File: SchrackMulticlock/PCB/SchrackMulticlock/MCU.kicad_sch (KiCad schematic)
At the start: 3 parts, among them U6 ESP32-S3-WROOM-2

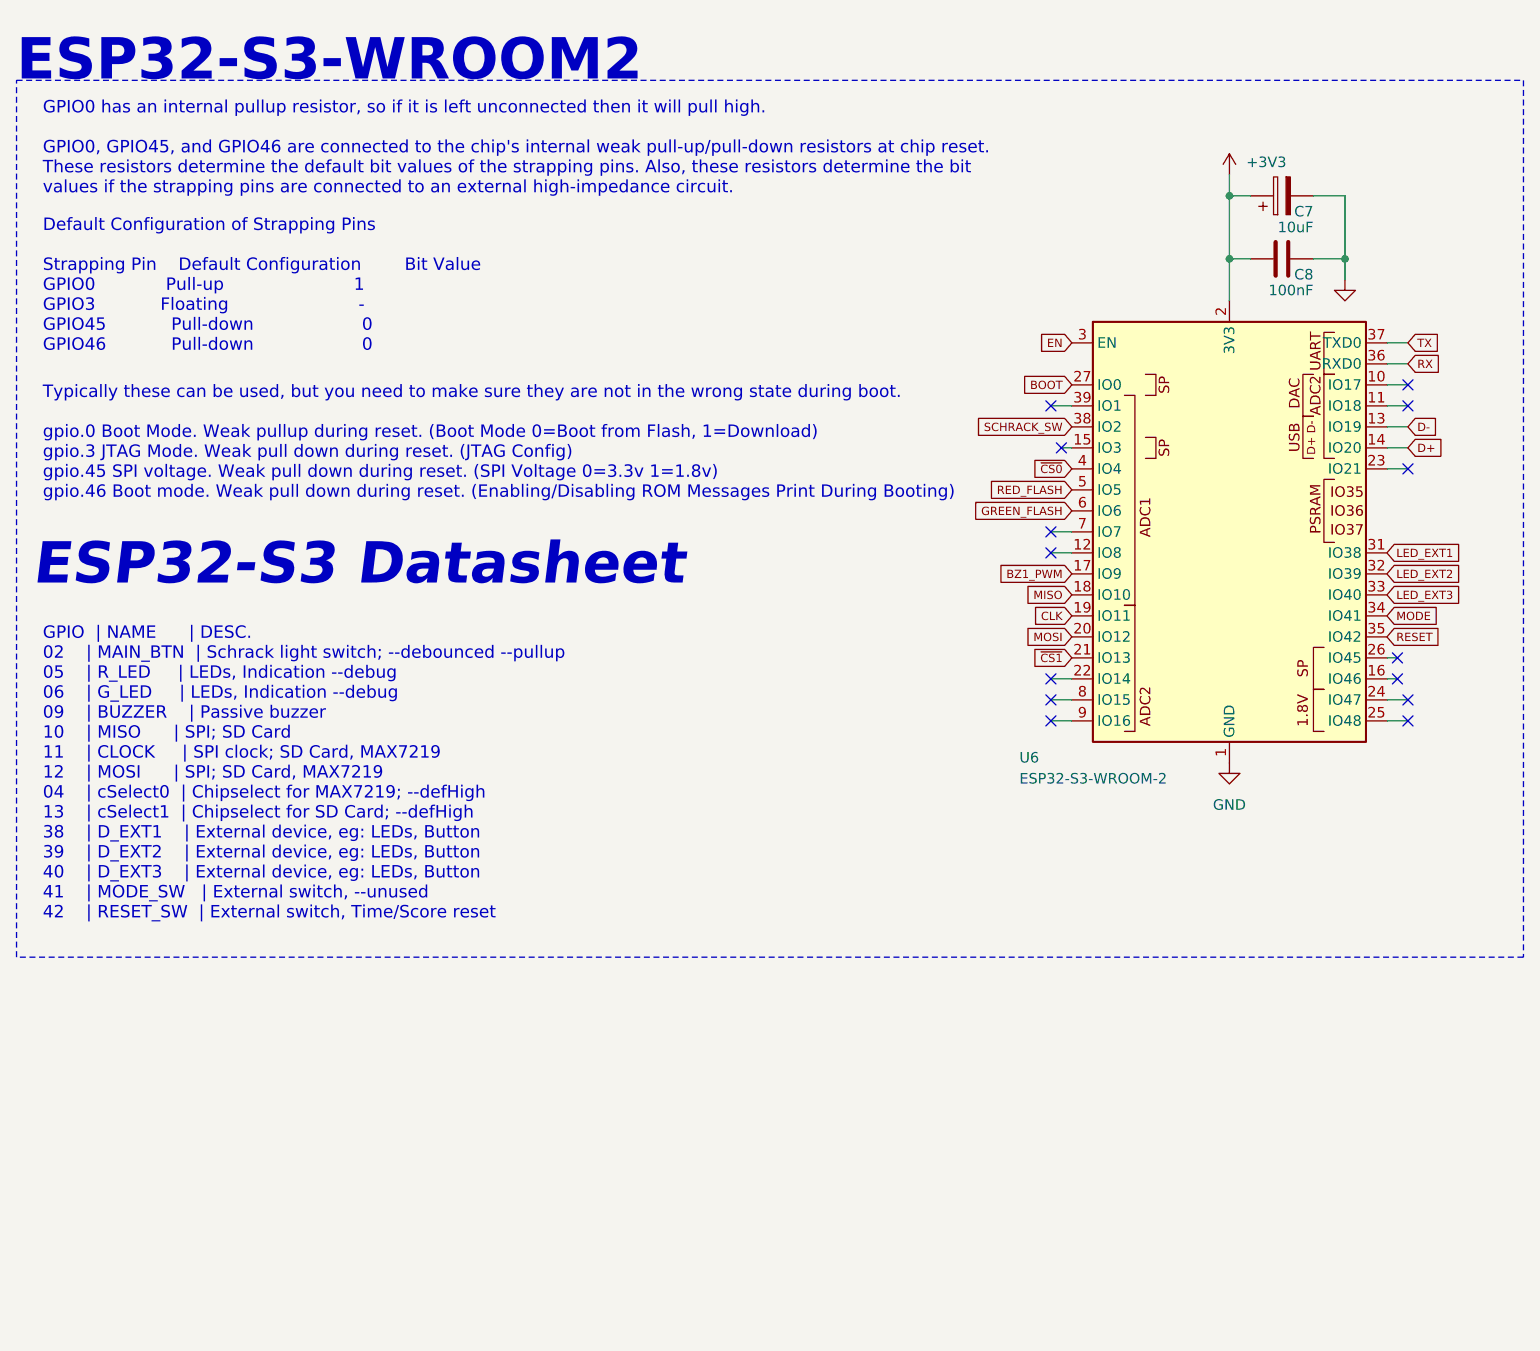
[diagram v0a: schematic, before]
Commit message: Stopwatch.h + Schematic update
Multiclock Scheamtic and code update
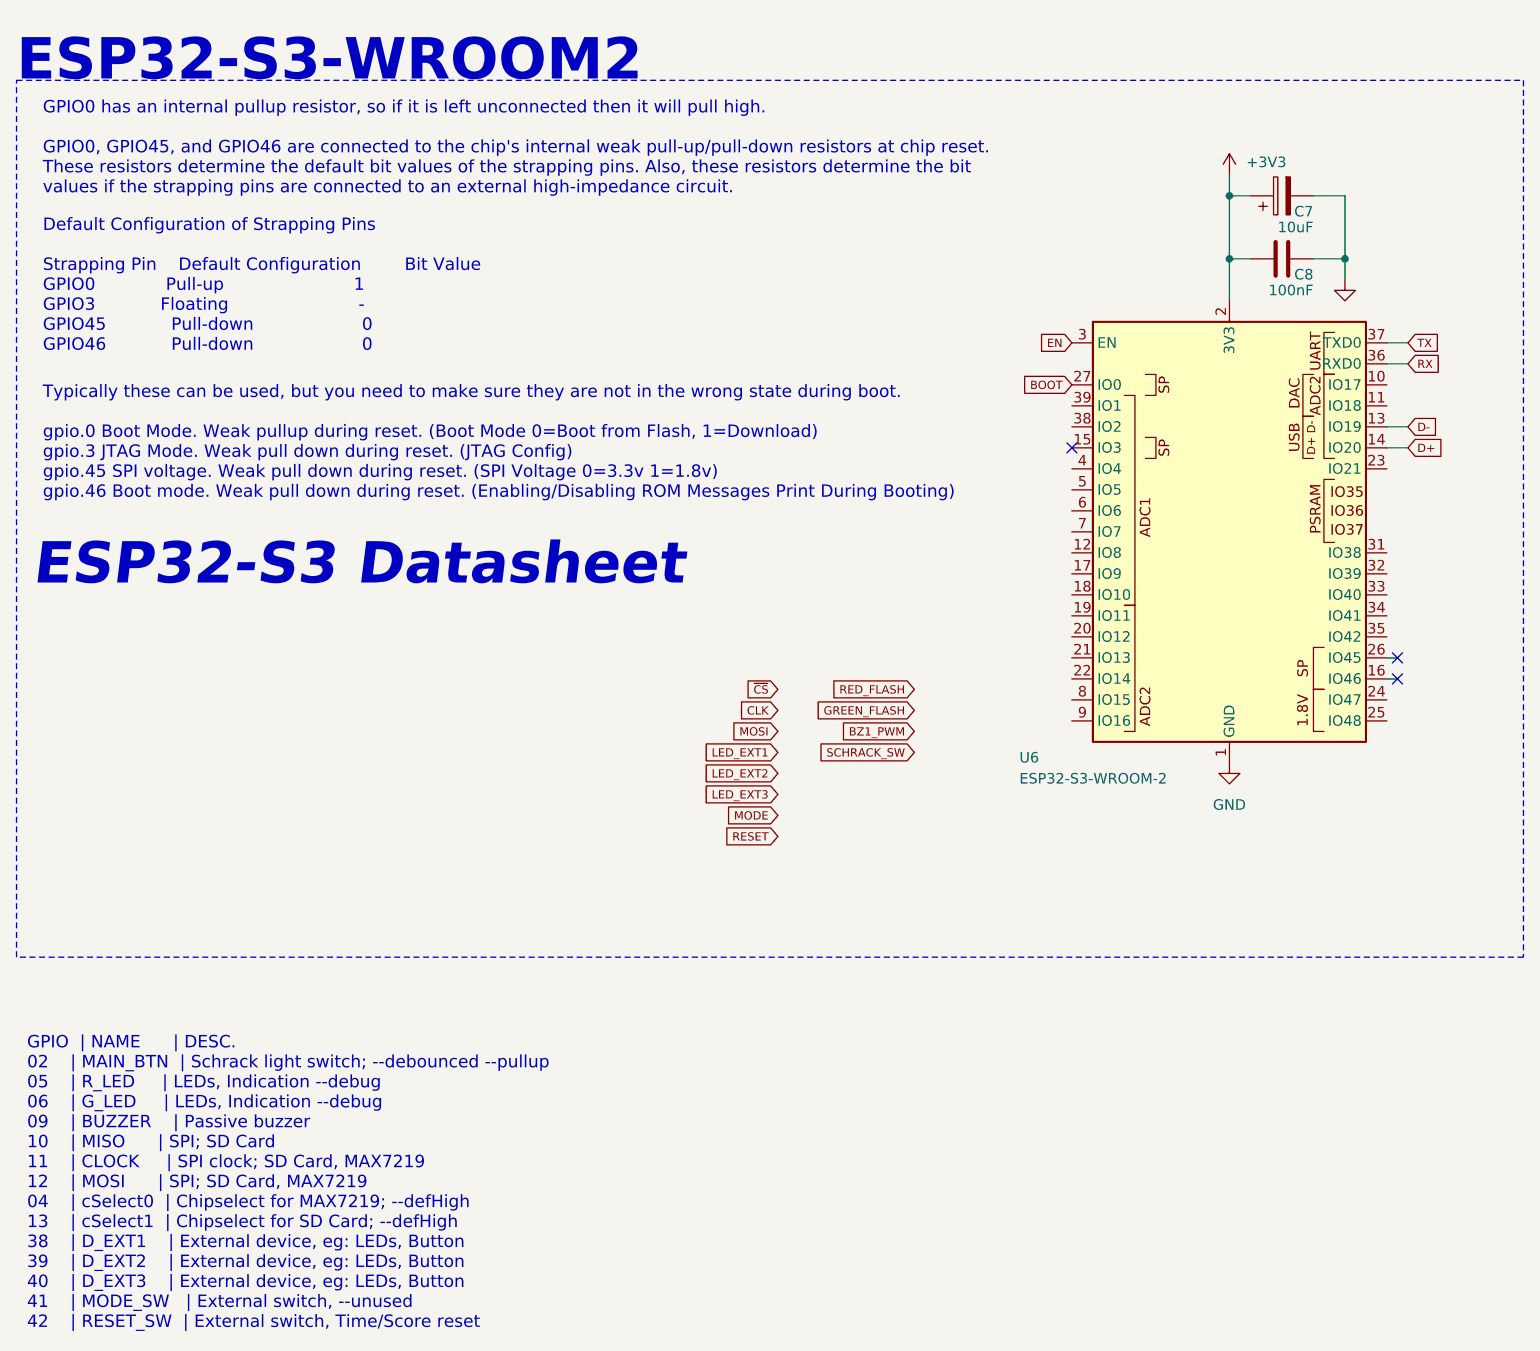
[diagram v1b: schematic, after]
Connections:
- net BZ1_PWM: no longer U6.17 (IO9)
- net CLK: no longer U6.19 (IO11)
- net GREEN_FLASH: no longer U6.6 (IO6)
- net LED_EXT1: no longer U6.31 (IO38)
- net LED_EXT2: no longer U6.32 (IO39)
- net LED_EXT3: no longer U6.33 (IO40)
- net MODE: no longer U6.34 (IO41)
- net MOSI: no longer U6.20 (IO12)
- net RED_FLASH: no longer U6.5 (IO5)
- net RESET: no longer U6.35 (IO42)
- net SCHRACK_SW: no longer U6.38 (IO2)
- net MISO: no longer names the net of U6.18 (IO10)
- net ~{CS0}: no longer names the net of U6.4 (IO4)
- net ~{CS1}: no longer names the net of U6.21 (IO13)
- no-connect marks 14 -> 3

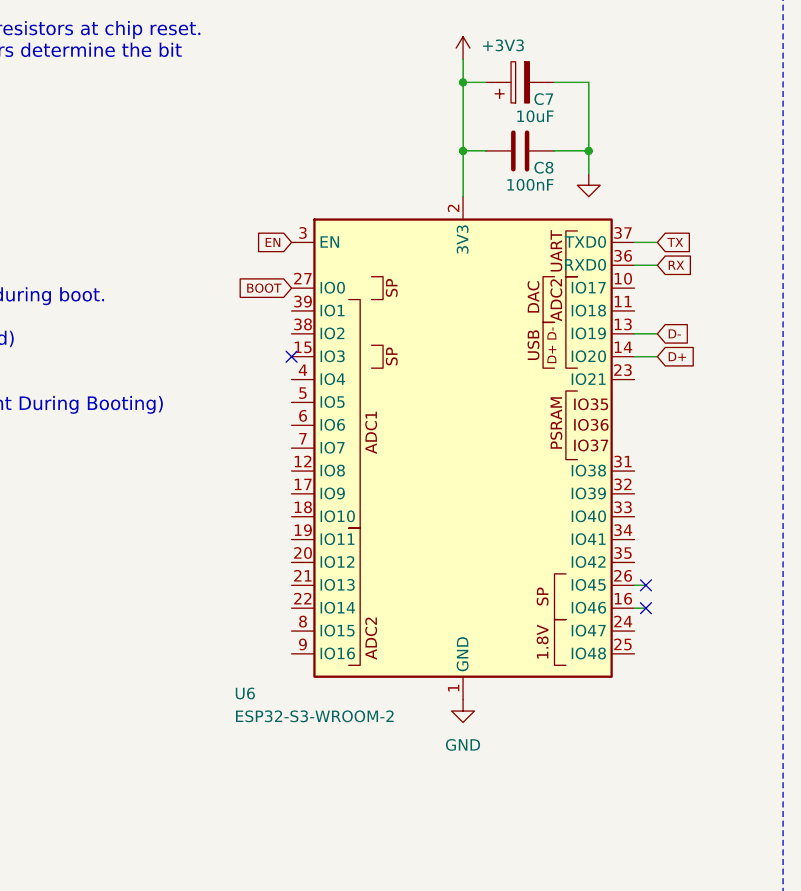
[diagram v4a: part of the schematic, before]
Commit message: SchrackMulticlock PCB final routing
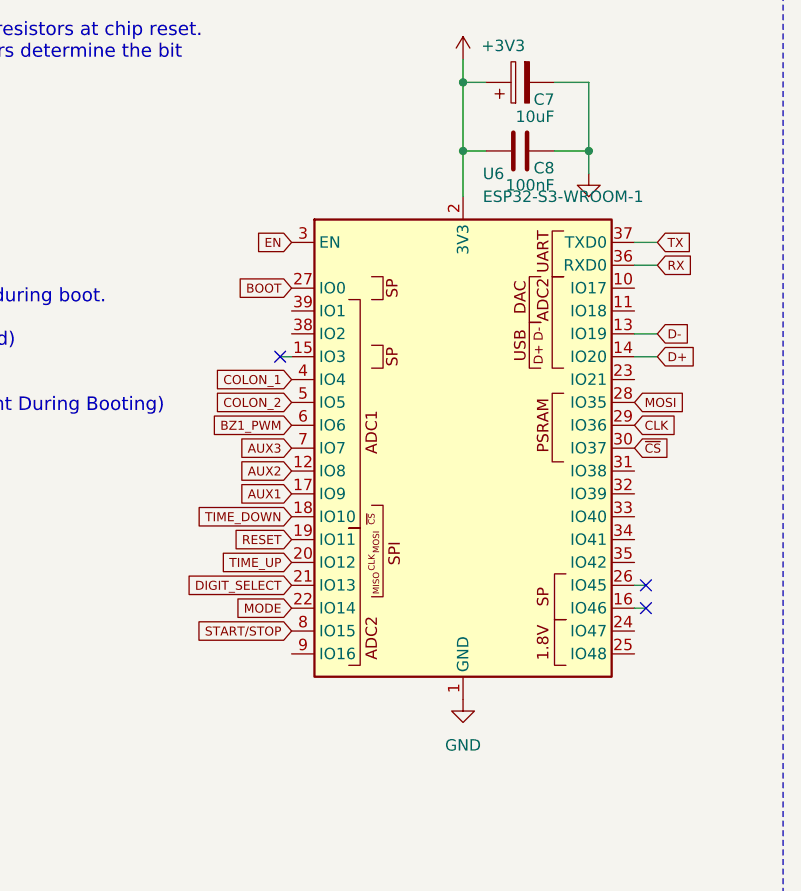
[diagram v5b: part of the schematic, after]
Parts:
- removed U6: ESP32-S3-WROOM-2, PCM_Espressif:ESP32-S3-WROOM-2, symbol sumec_sch_lib:ESP32-S3-WROOM-2_CUSTOM_made_by_bismarx
- added U6: ESP32-S3-WROOM-1, PCM_Espressif:ESP32-S3-WROOM-1, symbol sumec_sch_lib:ESP32-S3-WROOM-1_CUSTOM_made_by_bismarx
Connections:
- net +3V3: now also U6.2 (3V3)
- net BOOT: now also U6.27 (IO0)
- net D+: now also U6.14 (IO20)
- net D-: now also U6.13 (IO19)
- net EN: now also U6.3 (EN)
- net GND: now also U6.1 (GND), U6.40 (GND), U6.41 (GND)
- net RX: now also U6.36 (RXD0)
- net TX: now also U6.37 (TXD0)
- new net AUX1: U6.17 (IO9)
- new net AUX2: U6.12 (IO8)
- new net AUX3: U6.7 (IO7)
- new net BZ1_PWM: U6.6 (IO6)
- new net CLK: U6.29 (IO36)
- new net COLON_1: U6.4 (IO4)
- new net COLON_2: U6.5 (IO5)
- new net DIGIT_SELECT: U6.21 (IO13)
- new net MODE: U6.22 (IO14)
- new net MOSI: U6.28 (IO35)
- new net RESET: U6.19 (IO11)
- new net START/STOP: U6.8 (IO15)
- new net TIME_DOWN: U6.18 (IO10)
- new net TIME_UP: U6.20 (IO12)
- new net ~{CS}: U6.30 (IO37)

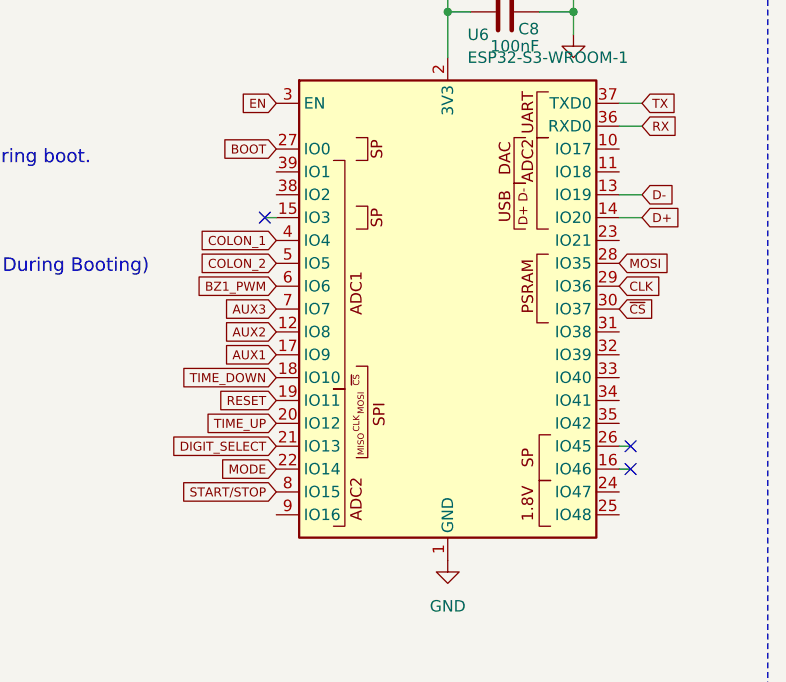
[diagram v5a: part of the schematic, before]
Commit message: Multiclock a lot of routing and layout
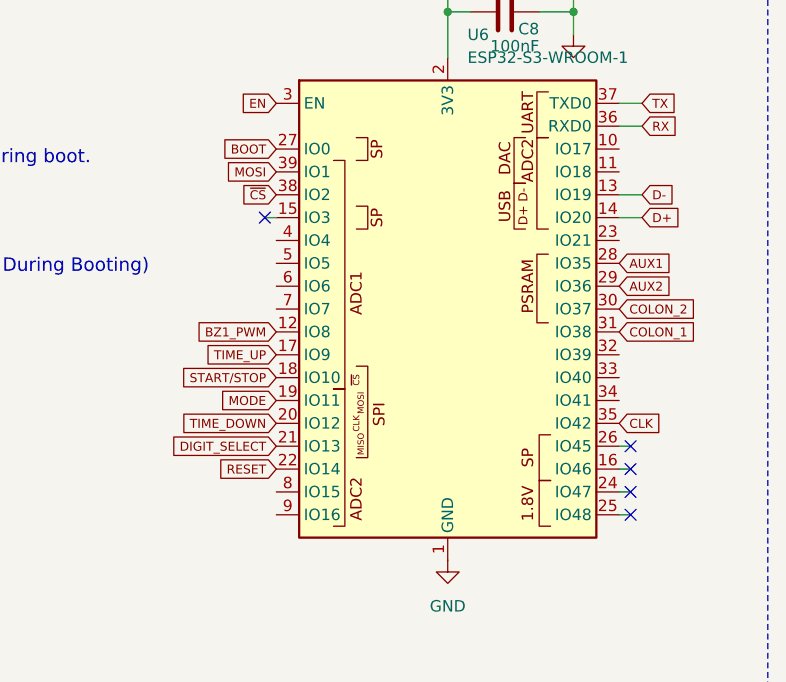
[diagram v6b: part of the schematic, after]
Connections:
- net AUX1: now also U6.28 (IO35); no longer U6.17 (IO9)
- net AUX2: now also U6.29 (IO36); no longer U6.12 (IO8)
- net BZ1_PWM: now also U6.12 (IO8); no longer U6.6 (IO6)
- net CLK: now also U6.35 (IO42); no longer U6.29 (IO36)
- net COLON_1: now also U6.31 (IO38); no longer U6.4 (IO4)
- net COLON_2: now also U6.30 (IO37); no longer U6.5 (IO5)
- net MODE: now also U6.19 (IO11); no longer U6.22 (IO14)
- net MOSI: now also U6.39 (IO1); no longer U6.28 (IO35)
- net RESET: now also U6.22 (IO14); no longer U6.19 (IO11)
- net START/STOP: now also U6.18 (IO10); no longer U6.8 (IO15)
- net TIME_DOWN: now also U6.20 (IO12); no longer U6.18 (IO10)
- net TIME_UP: now also U6.17 (IO9); no longer U6.20 (IO12)
- net ~{CS}: now also U6.38 (IO2); no longer U6.30 (IO37)
- net AUX3: no longer names the net of U6.7 (IO7)
- no-connect marks 3 -> 5
